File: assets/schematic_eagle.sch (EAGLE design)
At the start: 7 parts, among them J1 USB-TA-SLD

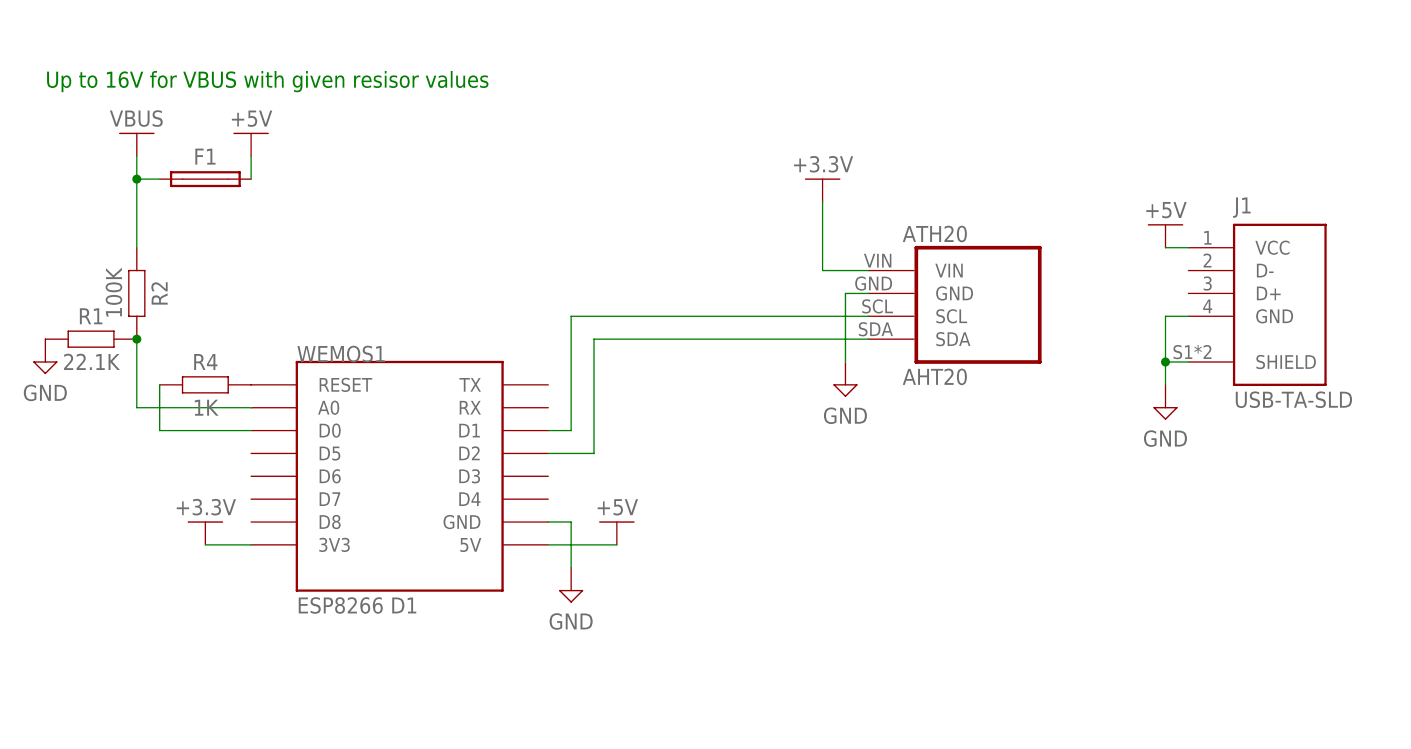
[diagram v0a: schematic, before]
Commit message: sensor type configurable
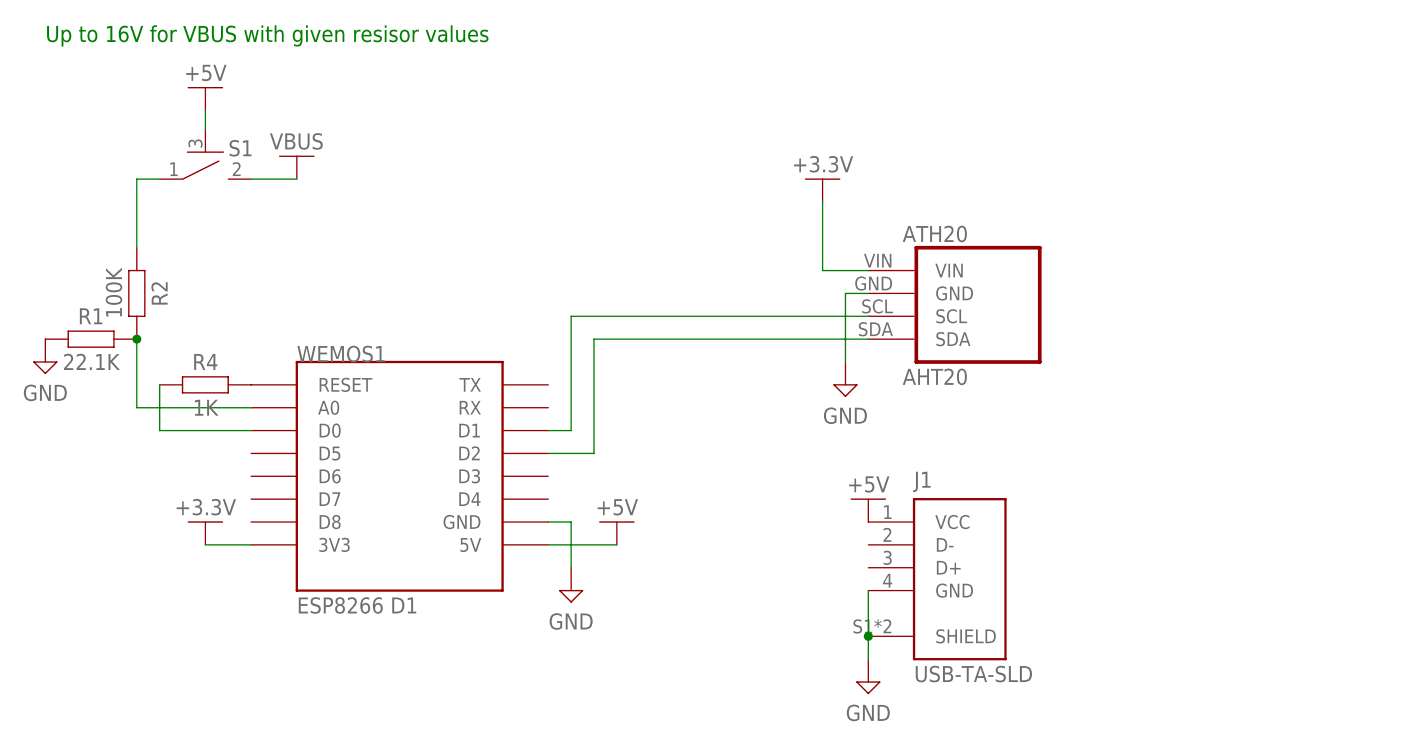
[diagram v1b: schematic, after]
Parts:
- removed F1: 1812L010, Bridge Pad:1812L010
- added S1: SMD_SWB3U-1100P(M)1100P(M), Jaisor Lib:SMD_SWB3U-1100P(M)1100P(M)
- WEMOS1: value (none) -> U1
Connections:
- new net N$6: R2.1, S1.1
- net +5V: now also S1.3; no longer F1.2
- net VBUS: now also S1.2; no longer F1.1, R2.1
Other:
- moved on the sheet: J1
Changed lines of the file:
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@@
 <parts>
 <part name="SUPPLY2" library="Power_Symbols" library_urn="urn:adsk.eagle:library:16502351" deviceset="GND" device="" value="GND"/>
-<part name="WEMOS1" library="esp8266modules" library_urn="urn:adsk.wipprod:fs.file:vf.rqZeGJ0zQBSPVXdJP1cbFw" deviceset="WEMOS-D1-MINI" device="">
+<part name="WEMOS1" library="esp8266modules" library_urn="urn:adsk.wipprod:fs.file:vf.rqZeGJ0zQBSPVXdJP1cbFw" deviceset="WEMOS-D1-MINI" device="" value="U1">
 <attribute name="CN" value="ESP8266 D1"/>
 </part>
-<part name="SUPPLY1" library="Power_Symbols" library_urn="urn:adsk.eagle:library:16502351" deviceset="GND" device="" value="GND"/>
-<part name="SUPPLY3" library="Power_Symbols" library_urn="urn:adsk.eagle:library:16502351" deviceset="+5V" device="" value="+5V"/>
 <part name="SUPPLY4" library="Power_Symbols" library_urn="urn:adsk.eagle:library:16502351" deviceset="+5V" device="" value="+5V"/>
 <part name="SUPPLY5" library="Power_Symbols" library_urn="urn:adsk.eagle:library:16502351" deviceset="+3.3V" device="" value="+3.3V"/>
@@
 <part name="SUPPLY8" library="Power_Symbols" library_urn="urn:adsk.eagle:library:16502351" deviceset="GND" device="" value="GND"/>
 <part name="SUPPLY9" library="Power_Symbols" library_urn="urn:adsk.eagle:library:16502351" deviceset="+5V" device="" value="+5V"/>
-<part name="F1" library="Bridge Pad" library_urn="urn:adsk.wipprod:fs.file:vf.oQWzh5Q1QJyMyLjqQiBJig" deviceset="1812L" device="" package3d_urn="urn:adsk.eagle:package:24934287/4" technology="010"/>
 <part name="R4" library="Resistor" library_urn="urn:adsk.eagle:library:16378527" deviceset="R" device="CHIP-0805(2012-METRIC)" package3d_urn="urn:adsk.eagle:package:16378559/5" technology="_" value="1K"/>
 <part name="R1" library="Resistor" library_urn="urn:adsk.eagle:library:16378527" deviceset="R" device="CHIP-0805(2012-METRIC)" package3d_urn="urn:adsk.eagle:package:16378559/5" technology="_" value="22.1K"/>
 <part name="R2" library="Resistor" library_urn="urn:adsk.eagle:library:16378527" deviceset="R" device="CHIP-0805(2012-METRIC)" package3d_urn="urn:adsk.eagle:package:16378559/5" technology="_" value="100K"/>
-<part name="J1" library="Jaisor Lib" library_urn="urn:adsk.wipprod:fs.file:vf._iimQKIpT1GV9qWvNx8InQ" deviceset="USB-TA-SLD" device="" package3d_urn="urn:adsk.eagle:package:46693770/4" value="USB-TA-SLD"/>
-<part name="ATH20" library="Jaisor Lib" library_urn="urn:adsk.wipprod:fs.file:vf._iimQKIpT1GV9qWvNx8InQ" deviceset="AHT20" device="" package3d_urn="urn:adsk.eagle:package:46694044/3" value="AHT20"/>
+<part name="ATH20" library="Jaisor Lib" library_urn="urn:adsk.wipprod:fs.file:vf._iimQKIpT1GV9qWvNx8InQ" deviceset="AHT20" device="" package3d_urn="urn:adsk.eagle:package:46694044/4" value="AHT20"/>
 <part name="SUPPLY10" library="Power_Symbols" library_urn="urn:adsk.eagle:library:16502351" deviceset="+V" device="" value="VBUS"/>
+<part name="S1" library="Jaisor Lib" library_urn="urn:adsk.wipprod:fs.file:vf._iimQKIpT1GV9qWvNx8InQ" deviceset="SMD_SW" device="1100P(M)" package3d_urn="urn:adsk.eagle:package:46901574/2" technology="B3U-1100P(M)" value="SMD_SWB3U-1100P(M)1100P(M)"/>
+<part name="J1" library="Jaisor Lib" library_urn="urn:adsk.wipprod:fs.file:vf._iimQKIpT1GV9qWvNx8InQ" deviceset="USB-TA-SLD" device="" package3d_urn="urn:adsk.eagle:package:46693770/5"/>
+<part name="SUPPLY11" library="Power_Symbols" library_urn="urn:adsk.eagle:library:16502351" deviceset="+5V" device="" value="+5V"/>
+<part name="SUPPLY1" library="Power_Symbols" library_urn="urn:adsk.eagle:library:16502351" deviceset="GND" device="" value="GND"/>
 </parts>
 <sheets>
 <sheet>
 <plain>
-<text x="-12.7" y="76.2" size="1.778" layer="91">Up to 16V for VBUS with given resisor values</text>
+<text x="-12.7" y="81.28" size="1.778" layer="91">Up to 16V for VBUS with given resisor values</text>
 </plain>
 <instances>
@@
 <instance part="WEMOS1" gate="D1" x="25.4" y="33.02" smashed="yes">
 <attribute name="NAME" x="15.24" y="45.72" size="1.778" layer="95"/>
-<attribute name="VALUE" x="17.78" y="17.78" size="1.778" layer="96"/>
 <attribute name="CN" x="15.24" y="17.78" size="1.778" layer="96"/>
-</instance>
-<instance part="SUPPLY1" gate="G$1" x="111.76" y="40.64" smashed="yes">
-<attribute name="VALUE" x="111.76" y="38.1" size="1.778" layer="96" align="top-center"/>
-</instance>
-<instance part="SUPPLY3" gate="G$1" x="111.76" y="58.42" smashed="yes">
-<attribute name="VALUE" x="111.76" y="63.5" size="1.778" layer="96" align="top-center"/>
 </instance>
 <instance part="SUPPLY4" gate="G$1" x="50.8" y="25.4" smashed="yes">
@@
 <attribute name="VALUE" x="-12.7" y="43.18" size="1.778" layer="96" align="top-center"/>
 </instance>
-<instance part="SUPPLY9" gate="G$1" x="10.16" y="68.58" smashed="yes">
-<attribute name="VALUE" x="10.16" y="73.66" size="1.778" layer="96" align="top-center"/>
-</instance>
-<instance part="F1" gate="G$1" x="5.08" y="66.04" smashed="yes">
-<attribute name="NAME" x="5.08" y="68.54" size="1.778" layer="95" align="center"/>
+<instance part="SUPPLY9" gate="G$1" x="5.08" y="73.66" smashed="yes">
+<attribute name="VALUE" x="5.08" y="78.74" size="1.778" layer="96" align="top-center"/>
 </instance>
 <instance part="R4" gate="G$1" x="5.08" y="43.18" smashed="yes">
@@
 <attribute name="VALUE" x="-5.08" y="53.34" size="1.778" layer="96" rot="R270" align="center"/>
 </instance>
-<instance part="J1" gate="G$1" x="124.46" y="53.34" smashed="yes">
-<attribute name="NAME" x="119.38" y="62.23" size="1.778" layer="95"/>
-<attribute name="VALUE" x="119.38" y="40.64" size="1.778" layer="96"/>
-</instance>
 <instance part="ATH20" gate="A" x="88.9" y="50.8" smashed="yes">
 <attribute name="NAME" x="82.55" y="59.055" size="1.778" layer="95"/>
 <attribute name="VALUE" x="82.55" y="43.18" size="1.778" layer="96"/>
 </instance>
-<instance part="SUPPLY10" gate="G$1" x="-2.54" y="71.12" smashed="yes">
-<attribute name="VALUE" x="-2.54" y="73.66" size="1.778" layer="96" align="top-center"/>
+<instance part="SUPPLY10" gate="G$1" x="15.24" y="68.58" smashed="yes">
+<attribute name="VALUE" x="15.24" y="71.12" size="1.778" layer="96" align="top-center"/>
+</instance>
+<instance part="S1" gate="G$1" x="5.08" y="68.58" smashed="yes">
+<attribute name="NAME" x="7.62" y="68.58" size="1.778" layer="95"/>
+</instance>
+<instance part="J1" gate="G$1" x="88.9" y="22.86" smashed="yes">
+<attribute name="NAME" x="83.82" y="31.75" size="1.778" layer="95"/>
+<attribute name="VALUE" x="83.82" y="10.16" size="1.778" layer="96"/>
+</instance>
+<instance part="SUPPLY11" gate="G$1" x="78.74" y="27.94" smashed="yes">
+<attribute name="VALUE" x="78.74" y="33.02" size="1.778" layer="96" align="top-center"/>
+</instance>
+<instance part="SUPPLY1" gate="G$1" x="78.74" y="10.16" smashed="yes">
+<attribute name="VALUE" x="78.74" y="7.62" size="1.778" layer="96" align="top-center"/>
 </instance>
 </instances>
@@
 <segment>
 <pinref part="SUPPLY1" gate="G$1" pin="GND"/>
-<wire x1="114.3" y1="50.8" x2="111.76" y2="50.8" width="0.1524" layer="91"/>
-<wire x1="111.76" y1="45.72" x2="111.76" y2="43.18" width="0.1524" layer="91"/>
-<wire x1="111.76" y1="50.8" x2="111.76" y2="45.72" width="0.1524" layer="91"/>
-<wire x1="111.76" y1="45.72" x2="114.3" y2="45.72" width="0.1524" layer="91"/>
-<junction x="111.76" y="45.72"/>
+<wire x1="78.74" y1="20.32" x2="78.74" y2="15.24" width="0.1524" layer="91"/>
+<wire x1="78.74" y1="15.24" x2="78.74" y2="12.7" width="0.1524" layer="91"/>
 <pinref part="J1" gate="G$1" pin="GND"/>
 <pinref part="J1" gate="G$1" pin="SHIELD"/>
+<junction x="78.74" y="15.24"/>
 </segment>
 </net>
 <net name="+5V" class="1">
-<segment>
-<pinref part="SUPPLY3" gate="G$1" pin="+5V"/>
-<wire x1="111.76" y1="58.42" x2="114.3" y2="58.42" width="0.1524" layer="91"/>
-<pinref part="J1" gate="G$1" pin="VCC"/>
-</segment>
 <segment>
 <pinref part="SUPPLY4" gate="G$1" pin="+5V"/>
@@
 <segment>
 <pinref part="SUPPLY9" gate="G$1" pin="+5V"/>
-<wire x1="10.16" y1="66.04" x2="10.16" y2="68.58" width="0.1524" layer="91"/>
-<pinref part="F1" gate="G$1" pin="2"/>
+<wire x1="5.08" y1="73.66" x2="5.08" y2="71.58" width="0.1524" layer="91"/>
+<pinref part="S1" gate="G$1" pin="3"/>
+</segment>
+<segment>
+<pinref part="J1" gate="G$1" pin="VCC"/>
+<pinref part="SUPPLY11" gate="G$1" pin="+5V"/>
 </segment>
 </net>
@@
 </segment>
 </net>
-<net name="VBUS" class="0">
-<segment>
-<pinref part="SUPPLY10" gate="G$1" pin="+V"/>
-<wire x1="-2.54" y1="68.58" x2="-2.54" y2="66.04" width="0.1524" layer="91"/>
+<net name="N$6" class="0">
+<segment>
 <wire x1="-2.54" y1="58.42" x2="-2.54" y2="66.04" width="0.1524" layer="91"/>
 <wire x1="-2.54" y1="66.04" x2="0" y2="66.04" width="0.1524" layer="91"/>
 <pinref part="R2" gate="G$1" pin="1"/>
-<pinref part="F1" gate="G$1" pin="1"/>
-<junction x="-2.54" y="66.04"/>
-</segment>
-</net>
+<pinref part="S1" gate="G$1" pin="1"/>
+</segment>
+</net>
+<net name="VBUS" class="0">
+<segment>
+<wire x1="10.16" y1="66.04" x2="15.24" y2="66.04" width="0.1524" layer="91"/>
+<pinref part="SUPPLY10" gate="G$1" pin="+V"/>
+<pinref part="S1" gate="G$1" pin="2"/>
+</segment>
+</net>
